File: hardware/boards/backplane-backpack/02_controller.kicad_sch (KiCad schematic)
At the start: 4 parts, among them J10 SWD, U1 STM32C092FCP6

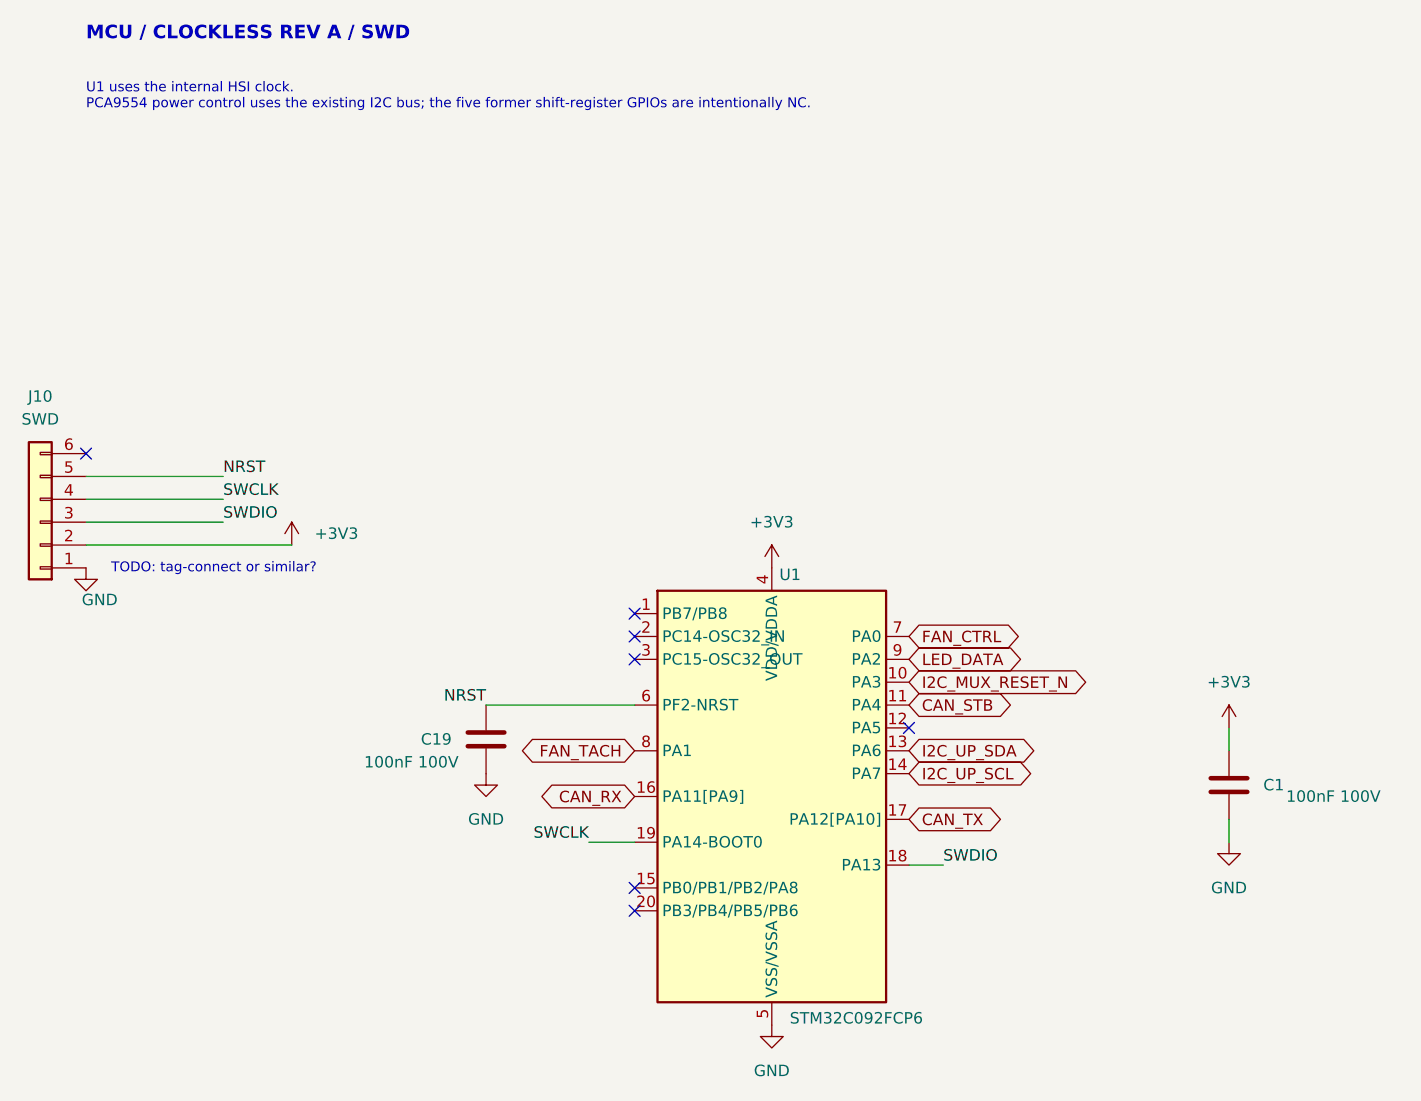
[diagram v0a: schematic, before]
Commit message: Simplify backpack backplane interface
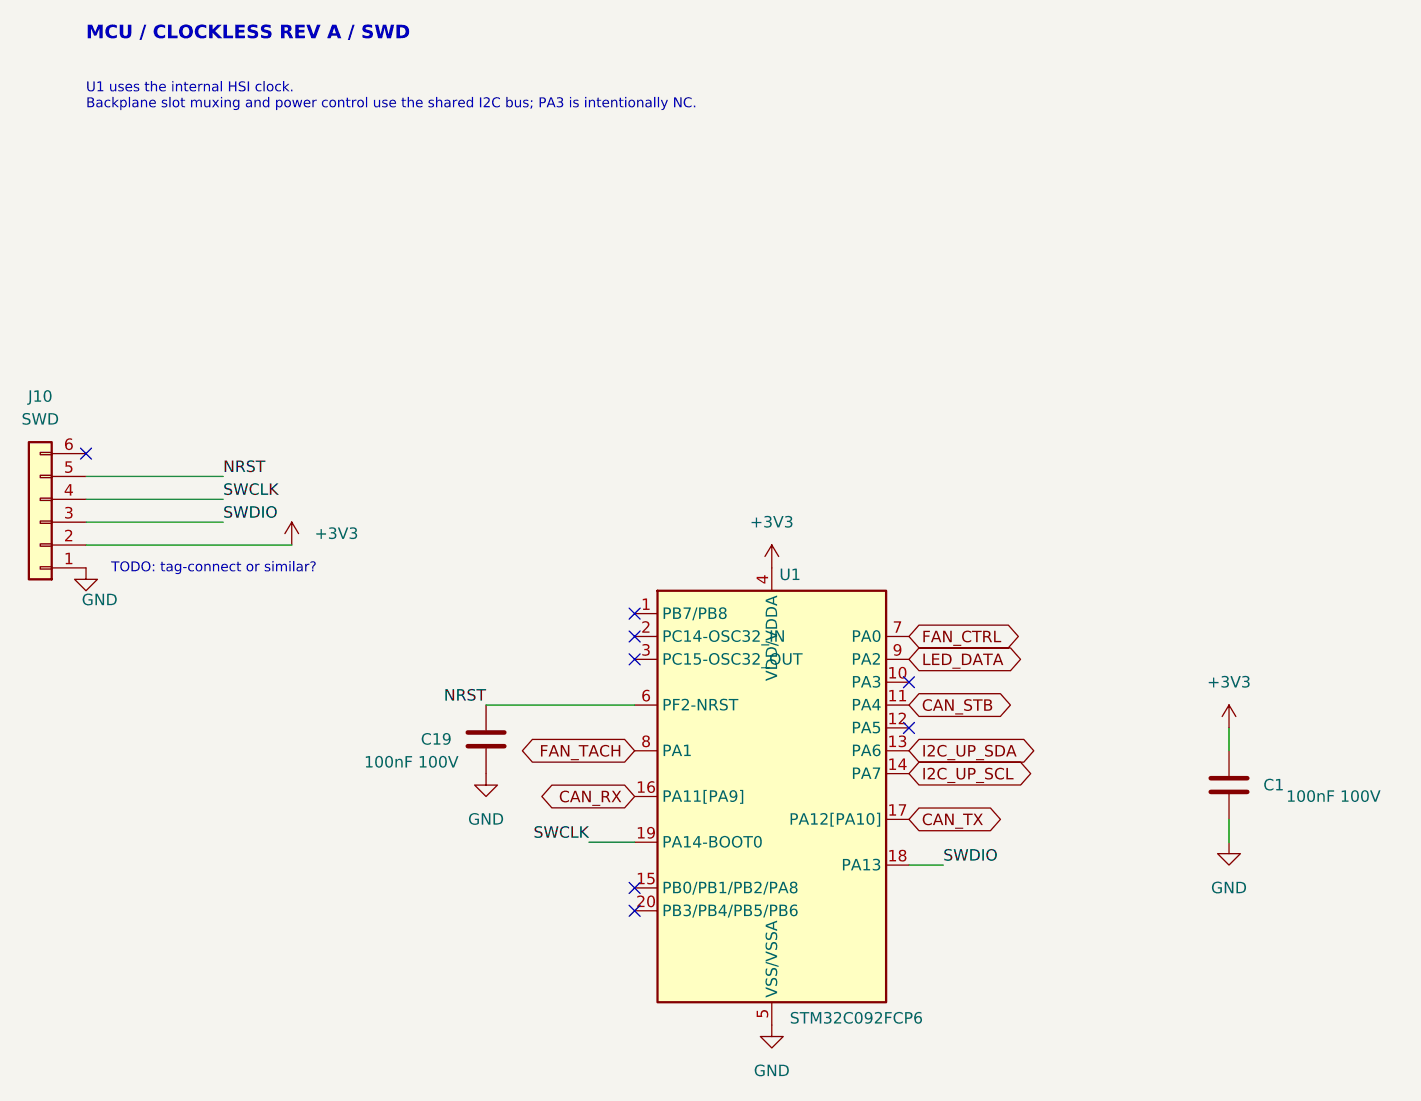
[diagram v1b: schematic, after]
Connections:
- net I2C_MUX_RESET_N: no longer names the net of U1.10 (PA3)
- no-connect marks 7 -> 8
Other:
- note added: "U1 uses the internal HSI clock. Backplane slot muxing and power control use the shared I2C bus; PA3 is intentionally NC."
- note removed: "U1 uses the internal HSI clock. PCA9554 power control uses the existing I2C bus; the five former shift-register GPIOs are intentionally NC."
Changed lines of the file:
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@@
 		)
 	)
-	(text "U1 uses the internal HSI clock.\nPCA9554 power control uses the existing I2C bus; the five former shift-register GPIOs are intentionally NC."
+	(text "U1 uses the internal HSI clock.\nBackplane slot muxing and power control use the shared I2C bus; PA3 is intentionally NC."
 		(exclude_from_sim no)
 		(at 25.4 25.4 0)
@@
 		)
 	)
-	(global_label "I2C_MUX_RESET_N"
-		(shape bidirectional)
-		(at 116.84 88.9 0)
-		(effects
-			(font
-				(size 1.27 1.27)
-			)
-			(justify left)
-		)
-		(property "Intersheetrefs" "${INTERSHEET_REFS}"
-			(at 116.84 88.9 0)
-			(hide yes)
-			(show_name no)
-			(do_not_autoplace no)
-			(effects
-				(font
-					(size 1.27 1.27)
-				)
-			)
-		)
-	)
 	(global_label "I2C_UP_SDA"
 		(shape bidirectional)
@@
 		)
 	)
-		(no_connect
+	(no_connect
 		(at 116.84 93.98)
 	)
@@
 		)
 	)
+	(no_connect
+		(at 116.84 88.9)
+	)
 	(sheet_instances

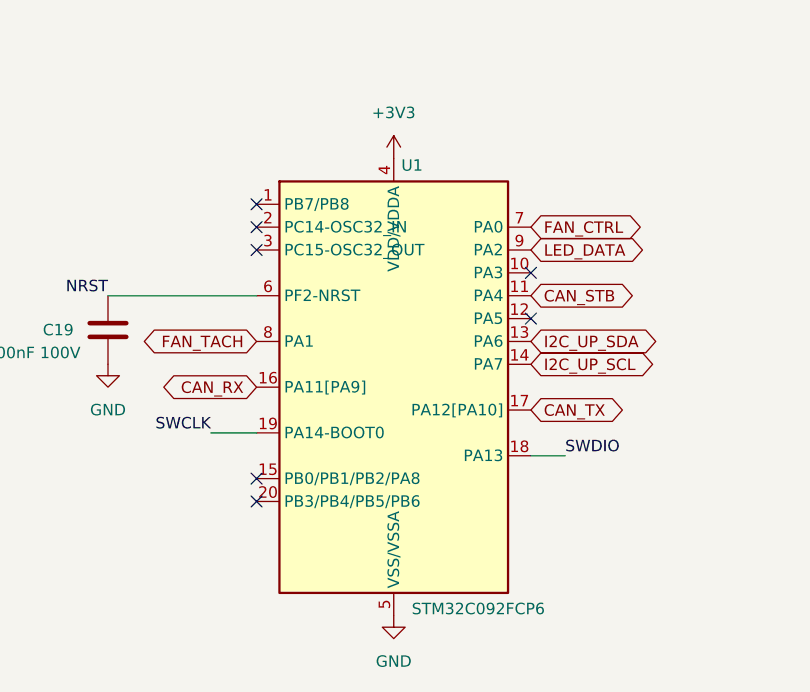
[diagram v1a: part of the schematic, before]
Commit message: Replace backpack MCU schematic with STM32C092GCU7
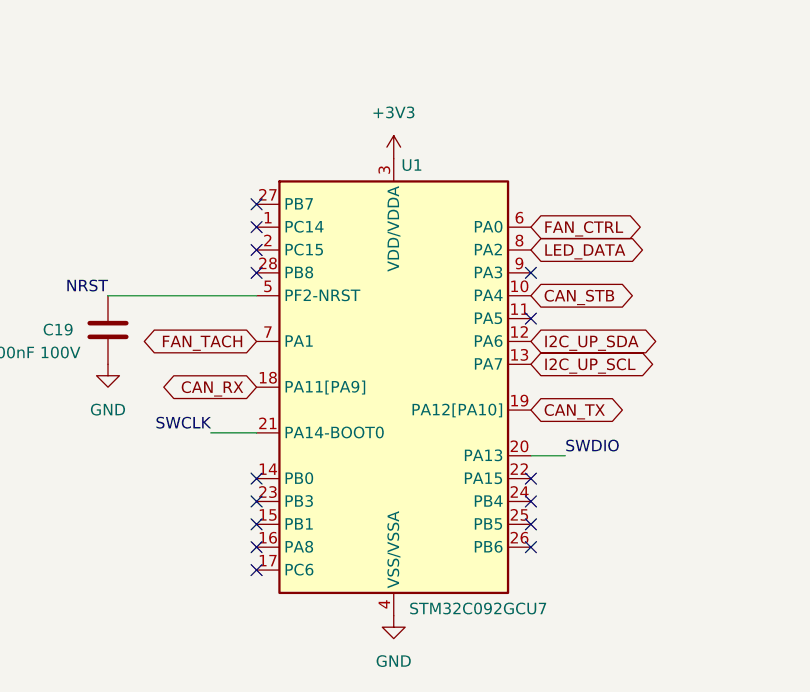
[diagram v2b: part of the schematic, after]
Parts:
- U1: value STM32C092FCP6 -> STM32C092GCU7; footprint Package_SO:TSSOP-20_4.4x6.5mm_P0.65mm -> Package_DFN_QFN:QFN-28_4x4mm_P0.5mm; symbol backplane-backpack:STM32C092FCP6 -> backplane-backpack:STM32C092GCU7; LCSC C44847704 -> (none); MPN STM32C092FCP6 -> STM32C092GCU7; Package TSSOP-20 -> UFQFPN-28
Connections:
- net +3V3: now also U1.3 (VDD/VDDA); no longer U1.4 (VDD/VDDA)
- net CAN_RX: now also U1.18 (PA11[PA9]); no longer U1.16 (PA11[PA9])
- net CAN_STB: now also U1.10 (PA4); no longer U1.11 (PA4)
- net CAN_TX: now also U1.19 (PA12[PA10]); no longer U1.17 (PA12[PA10])
- net FAN_CTRL: now also U1.6 (PA0); no longer U1.7 (PA0)
- net FAN_TACH: now also U1.7 (PA1); no longer U1.8 (PA1)
- net GND: now also U1.4 (VSS/VSSA); no longer U1.5 (VSS/VSSA)
- net I2C_UP_SCL: now also U1.13 (PA7); no longer U1.14 (PA7)
- net I2C_UP_SDA: now also U1.12 (PA6); no longer U1.13 (PA6)
- net LED_DATA: now also U1.8 (PA2); no longer U1.9 (PA2)
- net NRST: now also U1.5 (PF2-NRST); no longer U1.6 (PF2-NRST)
- net SWCLK: now also U1.21 (PA14-BOOT0); no longer U1.19 (PA14-BOOT0)
- net SWDIO: now also U1.20 (PA13); no longer U1.18 (PA13)
- no-connect marks 8 -> 16
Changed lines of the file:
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@@
 		(at 86.36 114.3)
+	)
+	(no_connect
+		(at 86.36 116.84)
+	)
+	(no_connect
+		(at 86.36 119.38)
+	)
+	(no_connect
+		(at 86.36 121.92)
+	)
+	(no_connect
+		(at 116.84 111.76)
+	)
+	(no_connect
+		(at 116.84 114.3)
+	)
+	(no_connect
+		(at 116.84 116.84)
+	)
+	(no_connect
+		(at 116.84 119.38)
+	)
+	(no_connect
+		(at 86.36 88.9)
 	)
 	(symbol
@@
 	)
 	(symbol
-		(lib_id "backplane-backpack:STM32C092FCP6")
+		(lib_id "backplane-backpack:STM32C092GCU7")
 		(at 101.6 101.6 0)
 		(unit 1)
@@
 			)
 		)
-		(property "Value" "STM32C092FCP6"
+		(property "Value" "STM32C092GCU7"
 			(at 110.998 126.238 0)
 			(show_name no)
@@
 			)
 		)
-		(property "Footprint" "Package_SO:TSSOP-20_4.4x6.5mm_P0.65mm"
+		(property "Footprint" "Package_DFN_QFN:QFN-28_4x4mm_P0.5mm"
 			(at 101.6 96.52 0)
 			(hide yes)
@@
 			)
 		)
-		(property "Datasheet" "https://www.st.com/resource/en/datasheet/stm32c092cc.pdf"
+		(property "Datasheet" "https://www.st.com/resource/en/datasheet/stm32c092gc.pdf"
 			(at 101.6 93.98 0)
 			(hide yes)
@@
 			)
 		)
-		(property "Description" "STM32C092FCP6 Cortex-M0+ MCU with FDCAN, TSSOP-20; project pin allocation"
+		(property "Description" "STM32C092GCU7 Cortex-M0+ MCU with FDCAN, UFQFPN-28; project pin allocation"
 			(at 101.6 91.44 0)
 			(hide yes)
@@
 			)
 		)
-		(property "MPN" "STM32C092FCP6"
+		(property "MPN" "STM32C092GCU7"
 			(at 101.6 101.6 0)
 			(hide yes)
@@
 			)
 		)
-		(property "LCSC" "C44847704"
+		(property "LCSC" ""
 			(at 101.6 101.6 0)
 			(hide yes)
@@
 			)
 		)
-		(property "Package" "TSSOP-20"
+		(property "Package" "UFQFPN-28"
 			(at 101.6 101.6 0)
 			(hide yes)
@@
 			)
 		)
+		(pin "27"
+		)
+		(pin "9"
+		)
+		(pin "10"
+		)
+		(pin "11"
+		)
+		(pin "12"
+		)
+		(pin "13"
+		)
+		(pin "14"
+		)
+		(pin "18"
+		)
+		(pin "19"
+		)
+		(pin "20"
+		)
+		(pin "21"
+		)
 		(pin "1"
 		)
-		(pin "10"
-		)
-		(pin "11"
-		)
-		(pin "12"
-		)
-		(pin "13"
-		)
-		(pin "14"
-		)
-		(pin "15"
-		)
-		(pin "16"
-		)
-		(pin "17"
-		)
-		(pin "18"
-		)
-		(pin "19"
+		(pin "23"
 		)
 		(pin "2"
 		)
-		(pin "20"
-		)
 		(pin "3"
 		)
@@
 		(pin "8"
 		)
-		(pin "9"
+(pin "15"
+		)
+(pin "16"
+		)
+(pin "17"
+		)
+(pin "22"
+		)
+(pin "24"
+		)
+(pin "25"
+		)
+(pin "26"
+		)
+(pin "28"
 		)
 		(instances
